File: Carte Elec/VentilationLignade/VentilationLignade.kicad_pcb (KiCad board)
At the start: 2 copper layers, 65 parts, among them P1 RelaisBoard1, P10 SDCard, P11 Codeur Rotatif, P12 Teensy Bottom, P13 EndStops1, P14 Teensy_Haut, P15 EndStops2, P16 Teensy_cote, P17 Retour 12V, P18 Masse_12V, P19 12V1, P2 Temp_Ext, P20 12V2, P21 12V_1et2, P22 Teensy_Bas, P23 Serial, P24 Temp_PuitC, P3 RelaisBoard2, P4 Temp_Int, P5 RelaisBoard3, P6 Temp_Chem, P7 RelaisBoard4, P8 RelaisBoard5, P9 TFT, SW1 Reset_Push, SW2 BackLight_On/ff, U2 OPTO-TRANSISTOR, U3 OPTO-TRANSISTOR, U4 OPTO-TRANSISTOR, U5 OPTO-TRANSISTOR, U6 OPTO-TRANSISTOR

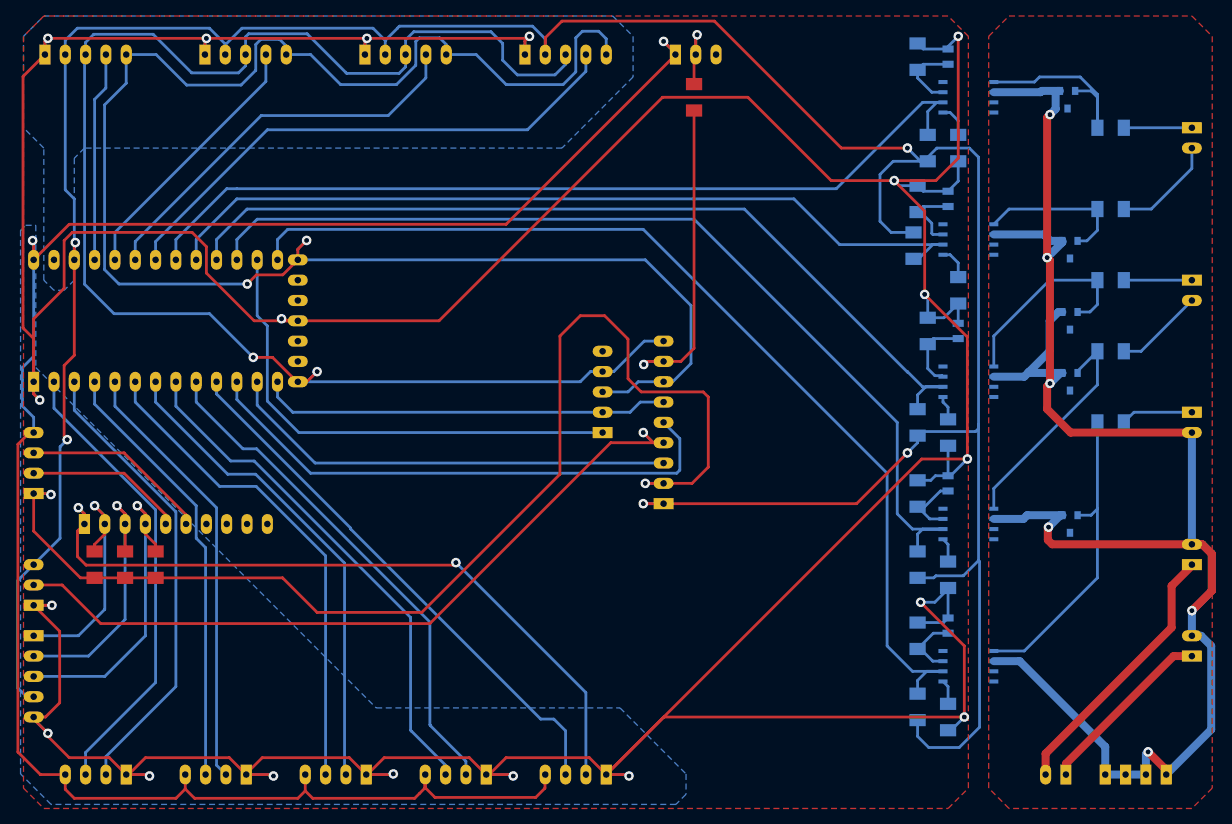
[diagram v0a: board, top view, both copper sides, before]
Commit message: Modification carte pour utiliser thermistors et real time clock.
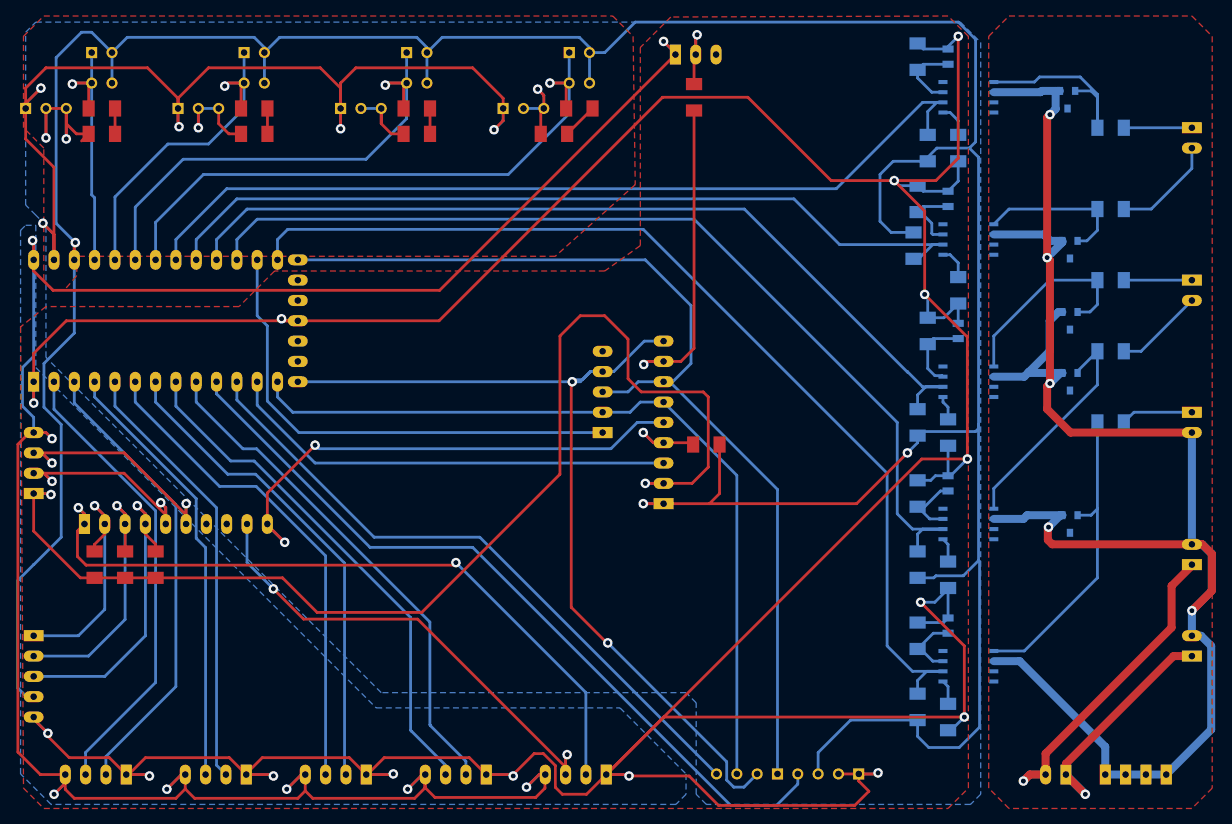
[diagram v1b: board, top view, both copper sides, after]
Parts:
- removed SW1: Reset_Push, SIL-3
- added C4: 1uF, C1, F.Cu at (193.7, 110.5)
- added C5: 1uF, C1, F.Cu at (173.4, 110.5)
- added C6: 1uF, C1, F.Cu at (153.0, 110.5)
- added C7: 1uF, C1, F.Cu at (134.0, 110.5)
- added P25: RT_CLK1, SIL-4, F.Cu at (224.8, 196.8)
- added P26: RT_CLK2, SIL-4, F.Cu at (214.6, 196.8)
- added R2: 4.47K, SM1206, F.Cu at (193.7, 113.7)
- added R24: 4.47K, SM1206, F.Cu at (173.4, 113.7)
- added R25: 91K, SM1206, F.Cu at (173.4, 116.8)
- added R26: 4.47K, SM1206, F.Cu at (153.0, 113.7)
- added R27: 91K, SM1206, F.Cu at (153.0, 116.8)
- added R28: 4.47K, SM1206, F.Cu at (134.0, 113.7)
- added R29: 91K, SM1206, F.Cu at (134.0, 116.8)
- added R3: 91K, SM1206, F.Cu at (190.5, 116.8)
- added R30: 100K, SM1206, F.Cu at (209.6, 155.7)
- added RV1: 10K, SIL-3, F.Cu at (186.7, 113.7)
- added RV2: 10K, SIL-3, F.Cu at (166.4, 113.7)
- added RV3: 10K, SIL-3, F.Cu at (146.1, 113.7)
- added RV4: 10K, SIL-3, F.Cu at (127.0, 113.7)
- C1, C2, C3: value C -> 0.1uF
- P2: value Temp_Ext -> PUIT_CAN; footprint SIL-5 -> SIL-2
- P24: value Temp_PuitC -> CHEMINEE; footprint SIL-5 -> SIL-2
- P4: value Temp_Int -> TEMP_EXT; footprint SIL-5 -> SIL-2
- P6: value Temp_Chem -> TEMP_INT; footprint SIL-5 -> SIL-2
- moved P24 59.2 mm to (134.0, 106.7)
- moved P2 20.5 mm to (193.7, 106.7)
- moved P4 20.1 mm to (173.4, 106.7)
- moved P6 19.8 mm to (153.0, 106.7)
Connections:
- P12 pad 10: (no net) -> TFT_DC
- P12 pad 9: (no net) -> 12V2_ON
- P14 pad 10: TCHEM_CS -> TCHEM_AN
- P14 pad 12: (no net) -> AGND
- P14 pad 7: TPUIT_CS -> TPUIT_AN
- P14 pad 8: TEXT_CS -> TEXT_AN
- P14 pad 9: TINT_CS -> TINT_AN
- P2 pad 1: GND -> TPUIT_AN
- P22 pad 10: 12V2_ON -> RTCLK_INTERRUPT
- P22 pad 11: TFT_DC -> RTCLK_CS
- P24 pad 1: GND -> TCHEM_AN
- P4 pad 1: GND -> TEXT_AN
- P6 pad 1: GND -> TINT_AN
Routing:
- net AGND: track 0.00 -> 132.8 mm, vias 0 -> 5
- net GND: track 807.9 -> 691.3 mm, vias 21 -> 17
- net RTCLK_INTERRUPT: track 0.00 -> 97.9 mm
- net SPI_SCK: track 215.0 -> 126.7 mm, vias 2 -> 0
- net N-0000026: track 96.2 -> 9.92 mm
- net RTCLK_CS: track 0.00 -> 81.6 mm
- net SPI_MISO: track 193.7 -> 113.6 mm
- net TPUIT_AN: track 0.00 -> 77.8 mm, vias 0 -> 1
- net TPUIT_CS: track 67.0 -> 0.00 mm
- net TEXT_AN: track 0.00 -> 62.2 mm, vias 0 -> 1
- net SPI_MOSI: track 51.5 -> 101.8 mm
- net TEXT_CS: track 50.0 -> 0.00 mm
- net +3.3V: track 385.9 -> 435.3 mm, vias 5 -> 3
- net TINT_AN: track 0.00 -> 44.0 mm, vias 0 -> 1
- net +5V: track 245.6 -> 285.0 mm, vias 2 -> 8
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- added copper zone on F.Cu, net AGND
